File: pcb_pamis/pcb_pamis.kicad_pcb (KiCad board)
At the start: 2 copper layers, 73 x 100.5 mm, 55 parts, among them J1 USB_C_Receptacle_USB2.0_16P, J10 Conn_01x03, J11 Conn_01x03, J12 Conn_02x06_Odd_Even, J2 1755736, J3 Conn_01x04, J4 Conn_01x04, J5 Conn_01x04, J6 Conn_01x05, J7 Conn_01x05, J8 Conn_01x05, J9 Conn_01x03, Q1 Q_NPN_BEC, Q2 Q_NPN_BEC, U1 ESP32-WROOM-32UE, U2 CP2102N-Axx-xQFN28, U3 TMC2209_SILENTSTEPSTICK, U4 TMC2209_SILENTSTEPSTICK, U5 TMC2209_SILENTSTEPSTICK

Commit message: ajout fixations
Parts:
- added H1: MountingHole_Pad, MountingHole:MountingHole_3.2mm_M3_ISO14580_Pad_TopBottom, F.Cu at (73.0, 31.0)
- added H2: MountingHole_Pad, MountingHole:MountingHole_3.2mm_M3_ISO14580_Pad_TopBottom, F.Cu at (73.0, 125.0)
- added H3: MountingHole_Pad, MountingHole:MountingHole_3.2mm_M3_ISO14580_Pad_TopBottom, F.Cu at (145.0, 125.0)
- added H4: MountingHole_Pad, MountingHole:MountingHole_3.2mm_M3_ISO14580_Pad_TopBottom, F.Cu at (145.0, 31.0)
- moved JP3 4.30 mm to (144.0, 116.7)
- moved J5 3.84 mm to (144.0, 113.5)
- renumbered RESET to SW1
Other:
- board size 73 x 100.5 mm -> 79 x 100.5 mm

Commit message: début routage PCB Pami
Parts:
- moved C9 2.65 mm to (108.5, 115.6)
- moved C10 1.00 mm to (134.0, 115.5)
- moved R8 0.71 mm to (122.0, 105.5), turned to -90 degrees
- moved C8 0.28 mm to (84.8, 115.6)
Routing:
- net TX_MOTEUR: track 0.00 -> 79.9 mm, vias 0 -> 2
- net EN: track 0.00 -> 36.6 mm, vias 0 -> 2
- net +3.3V: track 0.00 -> 33.0 mm, vias 0 -> 4
- net Net-(JP3-C): track 0.00 -> 21.0 mm
- net Net-(JP2-C): track 0.00 -> 19.9 mm
- net Net-(JP1-C): track 0.00 -> 19.6 mm
- net VBUS: track 0.00 -> 19.5 mm
- net Net-(R1-Pad2): track 0.00 -> 19.4 mm
- net IO0: track 0.00 -> 17.3 mm
- net RTS: track 0.00 -> 14.2 mm, vias 0 -> 3
- net DTR: track 0.00 -> 13.7 mm
- net Net-(J5-Pin_3): track 0.00 -> 11.8 mm
- net Net-(J1-CC2): track 0.00 -> 11.4 mm, vias 0 -> 2
- net Net-(Q1-B): track 0.00 -> 9.85 mm, vias 0 -> 2
- net TXD: track 0.00 -> 9.12 mm, vias 0 -> 2
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
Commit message: v1 routage
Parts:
- moved J10 2.67 mm to (119.0, 111.0), turned to 180 degrees
- moved R8 2.12 mm to (123.5, 104.0), turned to 0 degrees
- moved J5 2.00 mm to (144.0, 115.5)
- moved JP3 1.23 mm to (144.0, 118.0)
- moved R9 0.50 mm to (77.5, 103.5)
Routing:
- net +3.3V: track 33.0 -> 245.1 mm, vias 4 -> 7
- net VCC: track 0.00 -> 147.4 mm
- net STEP1: track 0.00 -> 72.0 mm, vias 0 -> 5
- net DIR1: track 0.00 -> 61.1 mm, vias 0 -> 6
- net STEP2: track 0.00 -> 54.7 mm, vias 0 -> 5
- net STEP3: track 0.00 -> 52.0 mm, vias 0 -> 8
- net /Drivers moteurs pas à pas/DISA3: track 3.63 -> 51.8 mm, vias 0 -> 3
- net Net-(BT1--): track 0.00 -> 47.4 mm
- net Net-(BT2--): track 0.00 -> 47.3 mm
- net DIR2: track 0.00 -> 41.5 mm, vias 0 -> 5
- net DIR3: track 0.00 -> 38.6 mm, vias 0 -> 4
- net GPIO12/MISO: track 0.00 -> 37.7 mm, vias 0 -> 2
- net GPIO15/CS: track 0.00 -> 36.4 mm, vias 0 -> 2
- net GPIO14/CLK: track 0.00 -> 30.8 mm, vias 0 -> 2
- net GPIO13/MOSI: track 0.00 -> 28.1 mm, vias 0 -> 2
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
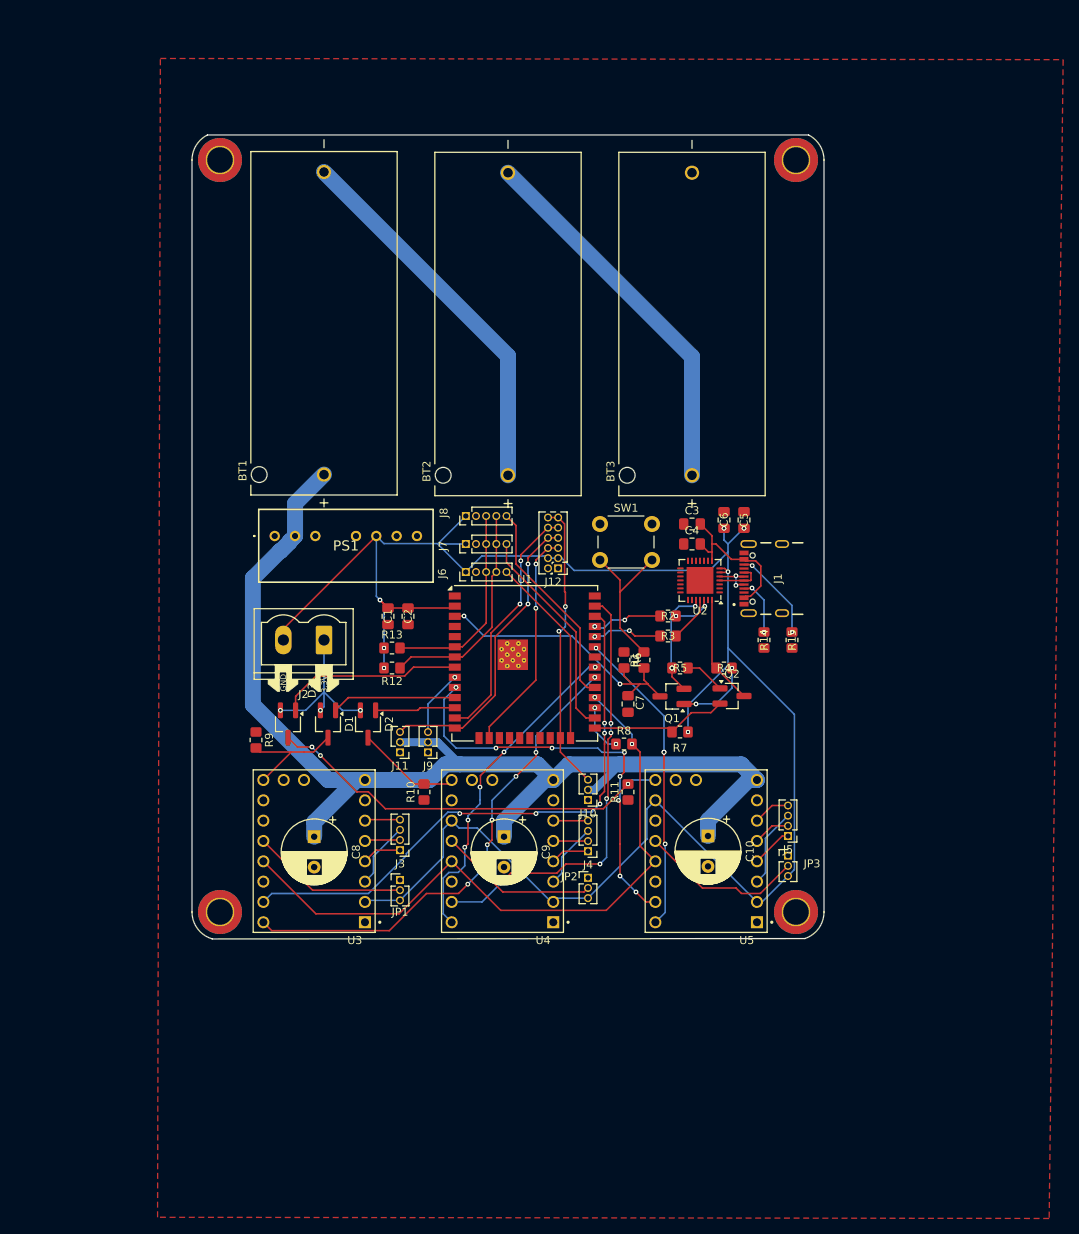
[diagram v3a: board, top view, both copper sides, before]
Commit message: routage avec 4 couches
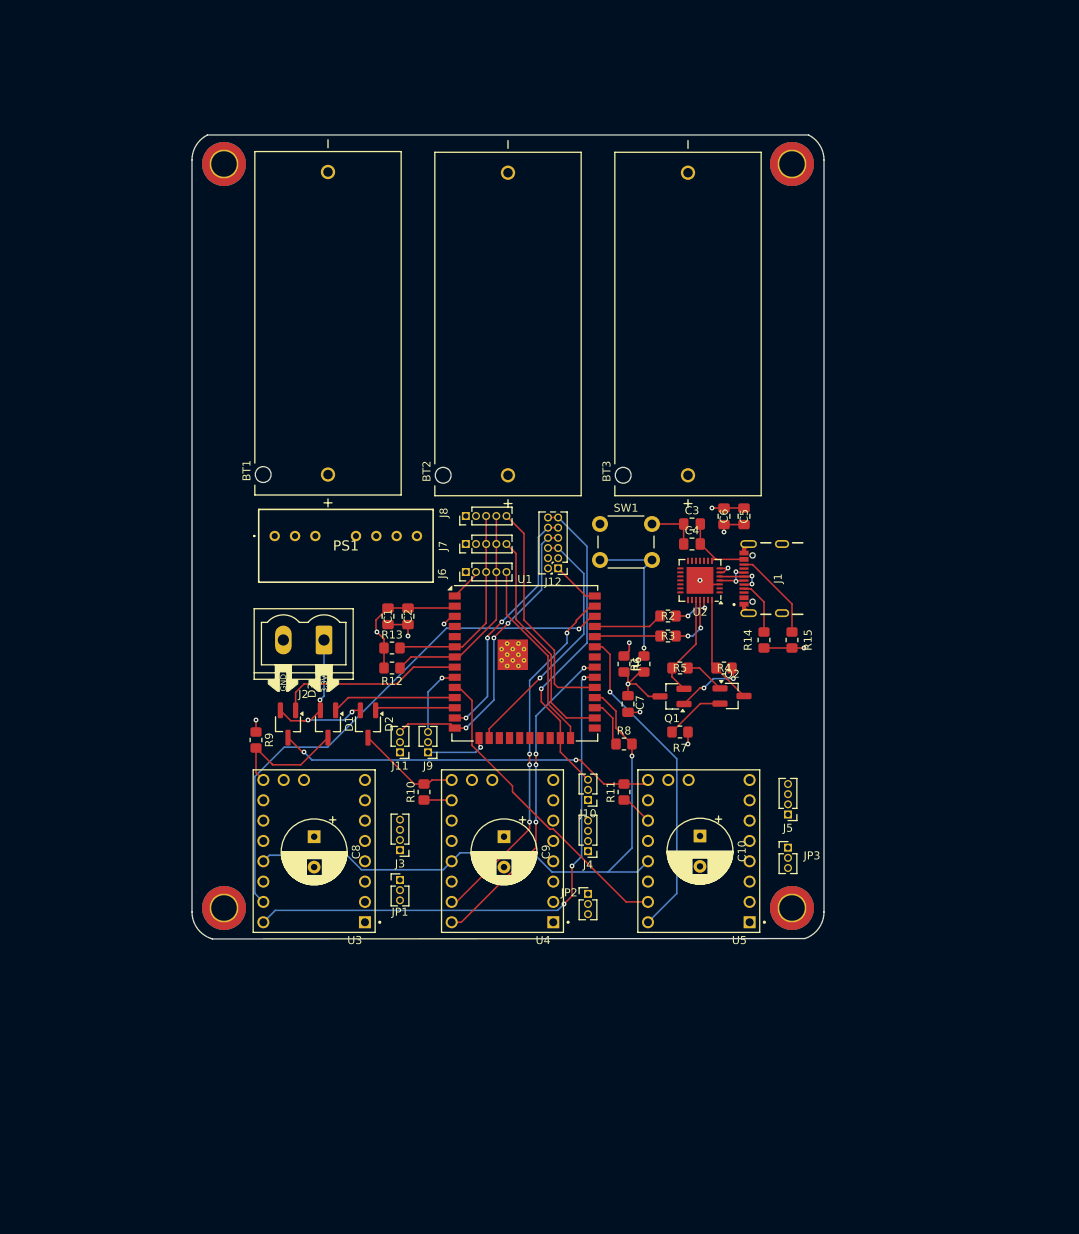
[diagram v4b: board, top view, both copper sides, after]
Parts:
- moved J5 2.69 mm to (144.0, 112.8)
- moved JP2 2.01 mm to (119.0, 122.7)
- moved C10 1.00 mm to (133.0, 115.5)
- moved JP3 1.00 mm to (144.0, 117.0)
- moved U5 0.92 mm to (132.8, 117.4)
- moved H1 0.71 mm to (73.5, 31.5)
- moved H2 0.71 mm to (73.5, 124.5)
- moved H3 0.71 mm to (144.5, 124.5)
- moved H4 0.71 mm to (144.5, 31.5)
- moved BT1 0.50 mm to (86.5, 51.4)
- moved BT3 0.50 mm to (131.5, 51.5)
- moved R1 0.50 mm to (126.0, 94.0)
- moved R11 0.50 mm to (123.5, 110.0)
- moved R6 0.50 mm to (123.5, 94.0)
- moved C5 0.46 mm to (138.5, 75.5)
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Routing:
- net +3.3V: track 245.1 -> 26.2 mm, vias 7 -> 5
- net GND: track 0.00 -> 53.8 mm, vias 0 -> 7
- net VCC: track 147.4 -> 168.0 mm
- net STEP3: track 52.0 -> 39.0 mm, vias 8 -> 0
- net VBUS: track 19.5 -> 9.31 mm
- net STEP2: track 54.7 -> 45.0 mm, vias 5 -> 4
- net IO0: track 17.3 -> 8.16 mm
- net Net-(J5-Pin_3): track 9.85 -> 18.9 mm
- net DIR1: track 61.1 -> 69.2 mm, vias 6 -> 3
- net TX_MOTEUR: track 83.4 -> 77.1 mm, vias 2 -> 1
- net STEP1: track 72.0 -> 67.0 mm, vias 5 -> 1
- net /Drivers moteurs pas à pas/DISA3: track 51.8 -> 47.6 mm, vias 3 -> 2
- net GPIO15/CS: track 36.4 -> 40.3 mm, vias 2 -> 1
- net GPIO13/MOSI: track 28.1 -> 31.3 mm, vias 2 -> 1
- net Net-(J5-Pin_1): track 5.19 -> 7.84 mm
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- added copper zone on In2.Cu, net +3.3V
- added copper zone on In1.Cu, net GND
- removed copper zone on F.Cu, net GND
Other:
- copper layers 2 -> 4

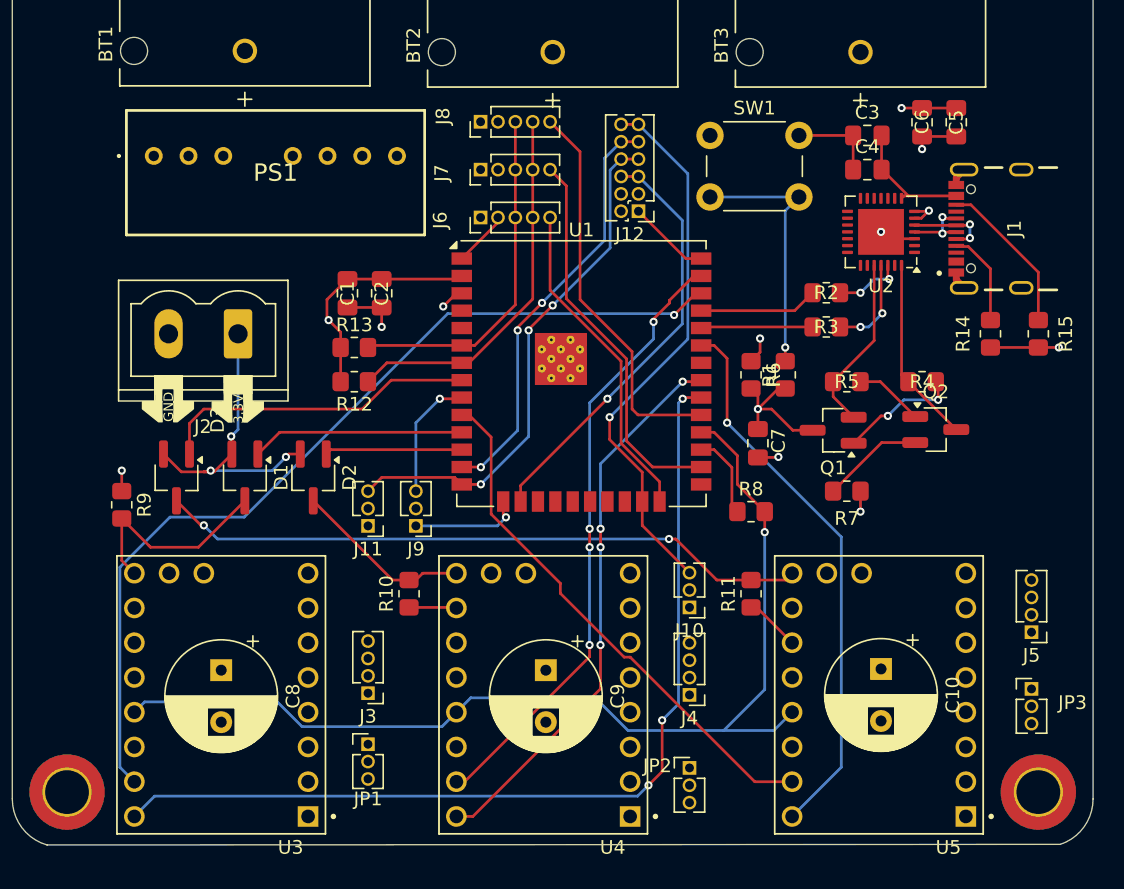
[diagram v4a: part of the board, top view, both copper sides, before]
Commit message: ajout indications
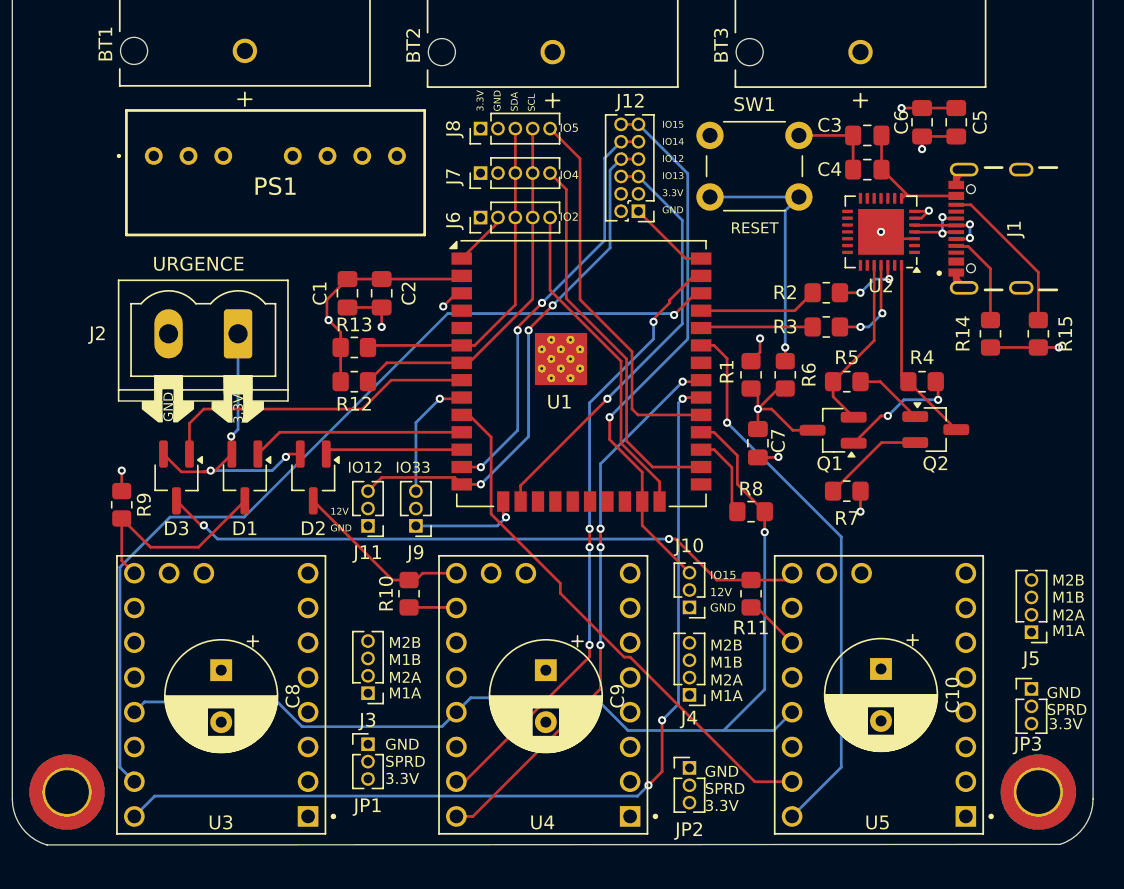
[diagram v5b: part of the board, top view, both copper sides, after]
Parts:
- moved J8 0.50 mm to (103.7, 76.0)
- moved J7 0.25 mm to (103.7, 79.2)
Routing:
- net SDA: track 25.4 -> 24.9 mm
- net SCL: track 27.5 -> 27.0 mm
- net GPIO5: track 28.7 -> 28.2 mm
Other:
- board text added: "12V"
- board text added: "3.3V"
- board text added: "GND"
- board text added: "IO12"
- board text added: "IO13"
- board text added: "IO14"
- board text added: "IO15"
- board text added: "IO2"
- board text added: "IO33"
- board text added: "IO4"
- board text added: "IO5"
- board text added: "M1A"
- board text added: "M1B"
- board text added: "M2A"
- board text added: "M2B"
- board text added: "RESET"
- board text added: "SCL"
- board text added: "SDA"
- board text added: "SPRD"
- board text added: "URGENCE"

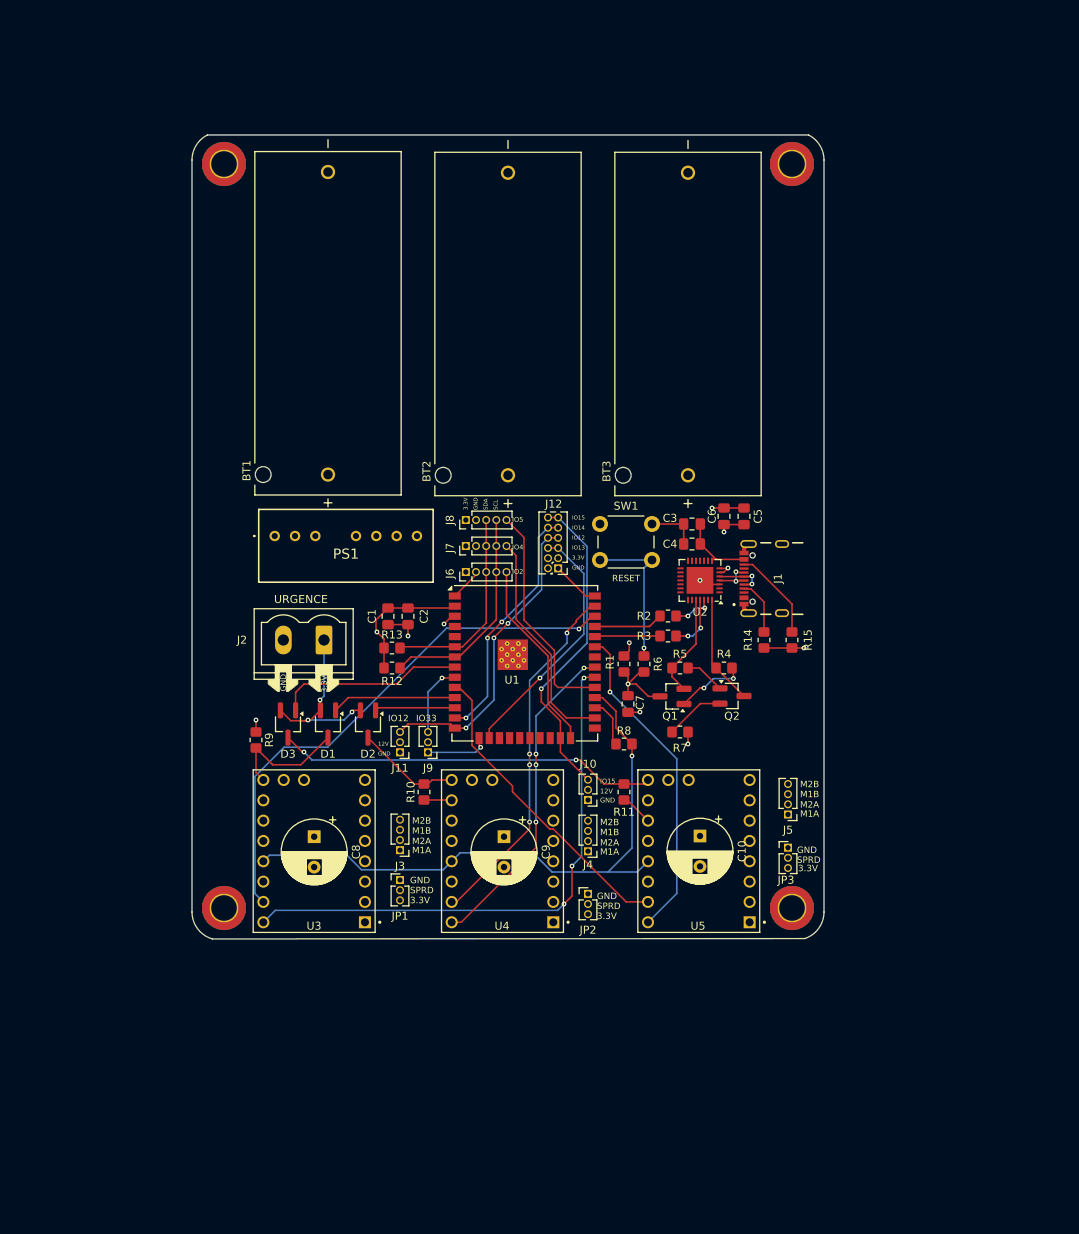
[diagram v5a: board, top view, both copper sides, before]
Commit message: legeres retouches, plan gnd couche top/bottom et suppression angles droits
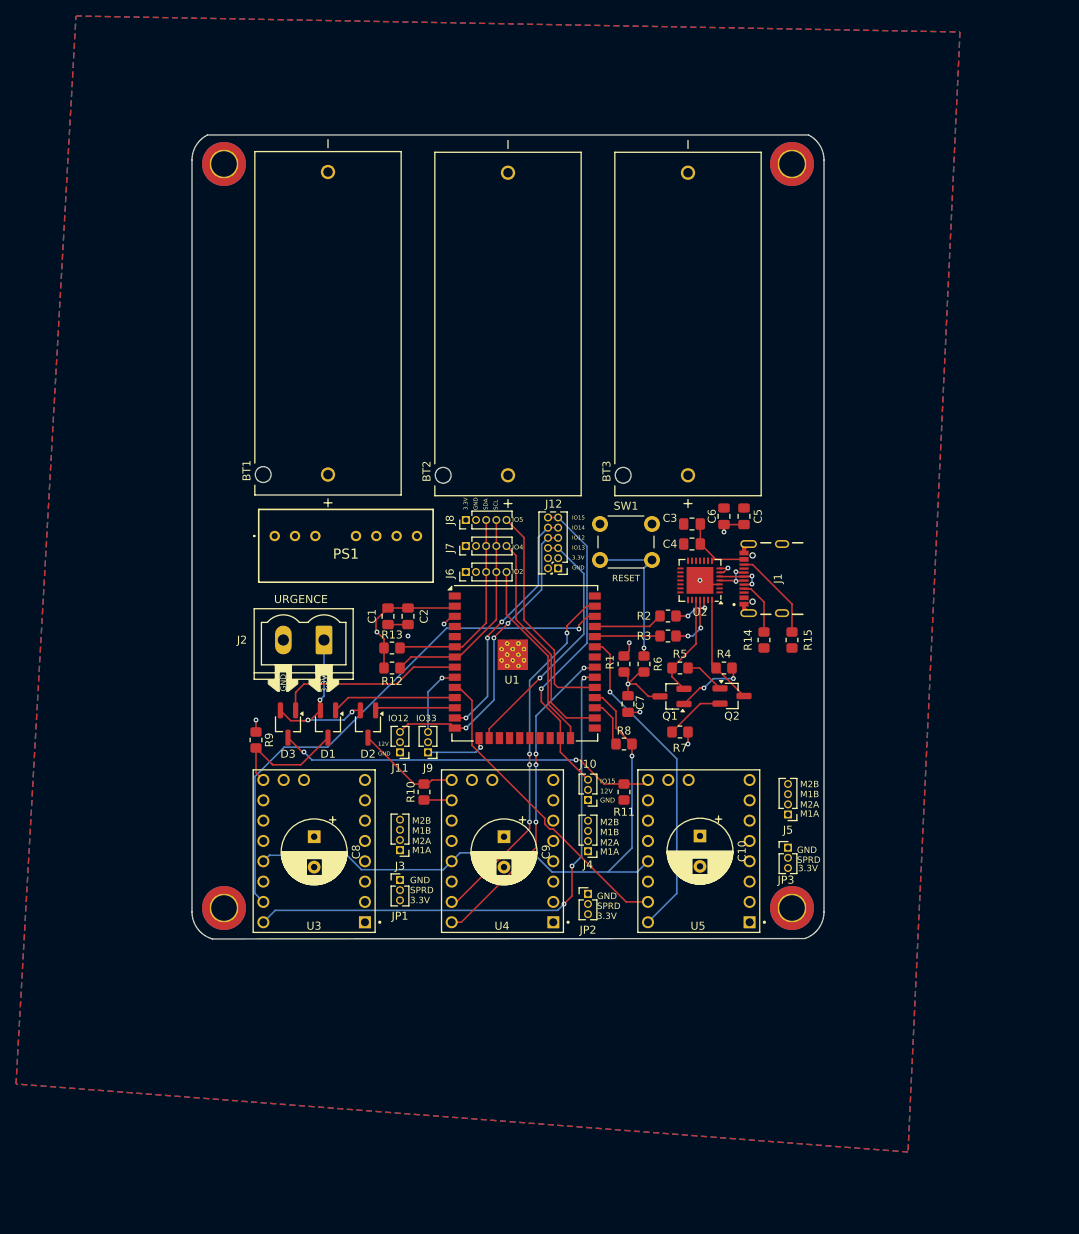
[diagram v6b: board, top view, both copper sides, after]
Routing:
- net GND: track 53.8 -> 23.5 mm, vias 7 -> 5
- net VCC: track 168.0 -> 172.5 mm
- added copper zone on B.Cu, net GND
- added copper zone on F.Cu, net GND
